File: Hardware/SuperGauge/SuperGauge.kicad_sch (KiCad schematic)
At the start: 1 part

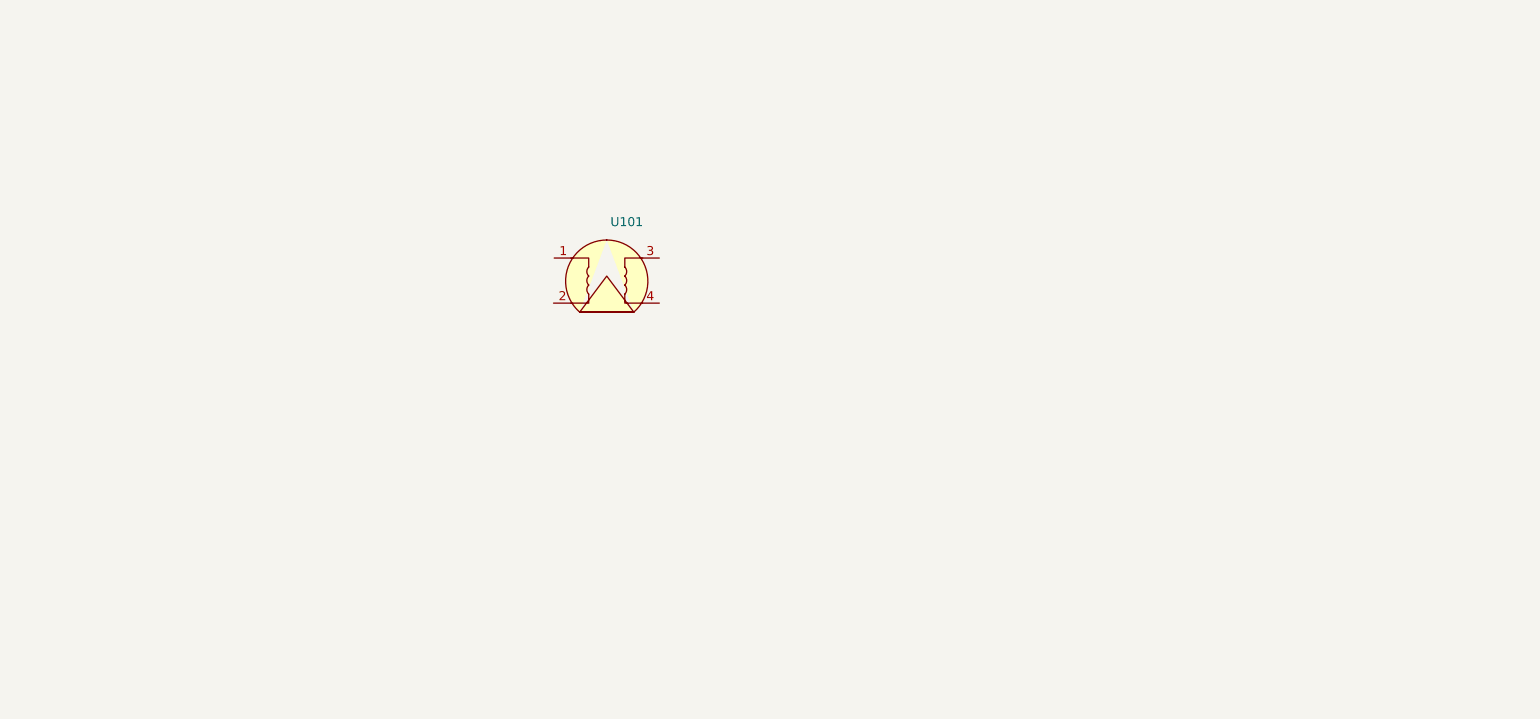
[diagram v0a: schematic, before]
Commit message: Added in MCU
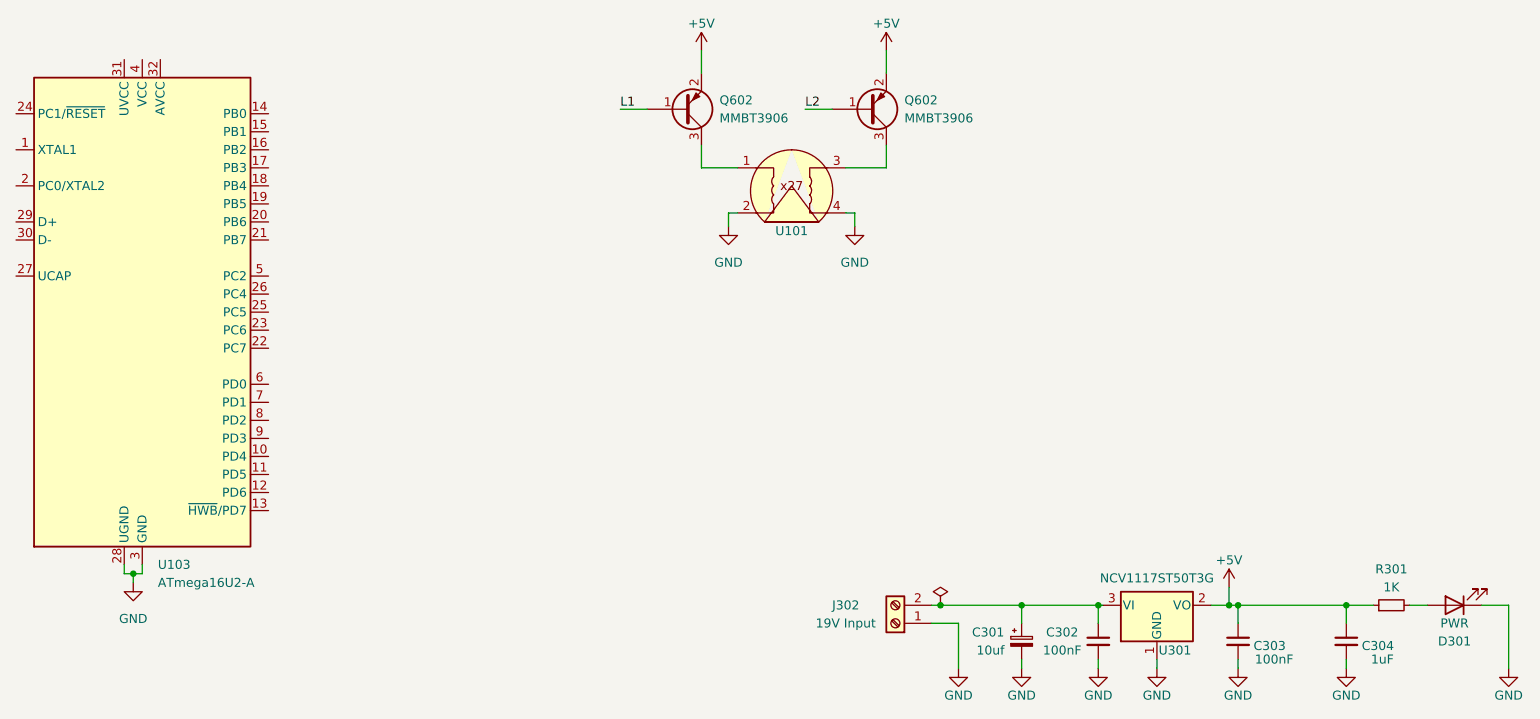
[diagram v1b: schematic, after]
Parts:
- added C301: 10uf, Capacitor_SMD:CP_Elec_4x3, symbol Device:C_Polarized_Small
- added C302, C303: 100nF, Capacitor_SMD:C_0805_2012Metric, symbol Device:C_Small
- added C304: 1uF, Capacitor_SMD:C_0805_2012Metric, symbol Device:C_Small
- added D301: PWR, LED_SMD:LED_0805_2012Metric, symbol Device:LED
- added J302: 19V Input, TerminalBlock_Phoenix:TerminalBlock_Phoenix_MKDS-3-2-5.08_1x02_P5.08mm_Horizontal, symbol Connector:Screw_Terminal_01x02
- added Q602 (x2): MMBT3906, Package_TO_SOT_SMD:SOT-23, symbol Transistor_BJT:MMBT3906
- added R301: 1K, Resistor_SMD:R_0805_2012Metric, symbol Device:R_Small
- added U103: ATmega16U2-A, Package_QFP:TQFP-32_7x7mm_P0.8mm, symbol MCU_Microchip_ATmega:ATmega16U2-A
- added U301: NCV1117ST50T3G, Package_TO_SOT_SMD:SOT-223, symbol Regulator_Linear:LM1117-5.0
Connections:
- net at U101.1: now also Q602.3 (C)
- net GND: now reaches U101.2
- net GND: now also U101.4, C301.2, C302.2, C303.2, C304.2, D301.1 (K), J302.1 (Pin_1), U103.28 (UGND), U103.3 (GND), U301.1 (GND)
- net at U101.3: now also Q602.3 (C)
- new net: C301.1, C302.1, J302.2 (Pin_2), U301.3 (VI)
- new net: D301.2 (A), R301.2
- new net +5V: C303.1, C304.1, Q602.2 (E), Q602.2 (E), R301.1, U301.2 (VO)
- new net L1: Q602.1 (B)
- new net L2: Q602.1 (B)

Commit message: More stuff
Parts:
- removed J302: 19V Input, TerminalBlock_Phoenix:TerminalBlock_Phoenix_MKDS-3-2-5.08_1x02_P5.08mm_Horizontal, symbol Connector:Screw_Terminal_01x02
- added D102, D103: BACKLIGHTING, LED_THT:LED_D5.0mm_Clear, symbol Device:LED
- added D301: STAT, LED_SMD:LED_0805_2012Metric, symbol Device:LED
- added H101, H102: MountingHole, MountingHole:MountingHole_2.5mm, symbol Mechanical:MountingHole
- added J102: MainConn, Connector_JST:JST_EH_B5B-EH-A_1x05_P2.50mm_Vertical, symbol Connector:Conn_01x05_Pin
- added R301 (x3): 1K, Resistor_SMD:R_0805_2012Metric, symbol Device:R_Small
- U103: value ATmega16U2-A -> ATmega16U2
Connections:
- net +5V: now also U103.4 (VCC), J102.4 (Pin_4), R301.1, R301.1
- net GND: now also D102.1 (K), D103.1 (K), D301.1 (K), J102.1 (Pin_1)
- net +12V: now reaches C301.1, C302.1, U301.3 (VI)
- net +12V: now also J102.5 (Pin_5)
- net at U103.6 (PD0): now also R301.1
- new net: D301.2 (A), R301.2
- new net: D102.2 (A), R301.2
- new net: D103.2 (A), R301.2
- new net SCL: J102.2 (Pin_2)
- new net SDA: J102.3 (Pin_3)
- no-connect marks 0 -> 2
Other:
- moved on the sheet: C304, D301, R301

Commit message: More PCB stuff
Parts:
- added C203, C204: 22pf, Capacitor_SMD:C_0603_1608Metric, symbol Device:C_Small
- added C303: 1u, Capacitor_SMD:C_0805_2012Metric, symbol Device:C_Small
- added J101: USBC, Connector_USB:USB_C_Receptacle_XKB_U262-16XN-4BVC11, symbol Connector:USB_C_Receptacle_USB2.0
- added R106, R107: 5K1, Resistor_SMD:R_0805_2012Metric, symbol Device:R_Small
- added Y101: Crystal_GND24, Crystal:Crystal_SMD_3225-4Pin_3.2x2.5mm, symbol Device:Crystal_GND24
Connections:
- net +5V: now also U103.32 (AVCC), J101.A4 (VBUS), J101.A9 (VBUS), J101.B4 (VBUS), J101.B9 (VBUS)
- net GND: now also C203.2, C204.2, C303.2, J101.A1 (GND), J101.A12 (GND), J101.B1 (GND), J101.B12 (GND), J101.S1 (SHIELD), R106.1, R107.1, Y101.2, Y101.4
- net XTAL1: now reaches U103.1 (XTAL1)
- net XTAL1: now also C204.1, Y101.3
- net XTAL2: now reaches U103.2 (PC0/XTAL2)
- net XTAL2: now also C203.1, Y101.1
- net at U103.27 (UCAP): now also C303.1
- net USB+: now reaches U103.29 (D+)
- net USB+: now also J101.A6 (D+), J101.B6 (D+)
- net USB-: now reaches U103.30 (D-)
- net USB-: now also J101.A7 (D-), J101.B7 (D-)
- new net: J101.A5 (CC1), R107.2
- new net: J101.B5 (CC2), R106.2
- no-connect marks 2 -> 4
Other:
- note added: "16pf = (22pf)/2+5pf"
- note added: "Consider not lol"
- note added: "USB"
- moved on the sheet: C303, D301, R301, U103

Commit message: Stuff
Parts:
- removed H101, H102: MountingHole, MountingHole:MountingHole_2.5mm, symbol Mechanical:MountingHole
- added J201: Tag Connect, Connector:Tag-Connect_TC2050-IDC-FP_2x05_P1.27mm_Vertical, symbol Connector_Generic:Conn_02x05_Odd_Even
- added R301 (x2): 22R, Resistor_SMD:R_0805_2012Metric, symbol Device:R_Small
- added R301: 10k, Resistor_SMD:R_0805_2012Metric, symbol Device:R_Small
- U103: LCSC# (none) -> C59019
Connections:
- net +5V: now also U103.31 (UVCC), J201.2 (Pin_2), R301.2
- net GND: now also J201.10 (Pin_10)
- net L1: now also U103.7 (PD1)
- net L2: now also U103.8 (PD2)
- net USB+: now also R301.1; no longer U103.29 (D+)
- net USB-: now also R301.1; no longer U103.30 (D-)
- net ICSP_SCK: now reaches U103.15 (PB1)
- net ICSP_SCK: now also J201.7 (Pin_7)
- net ICSP_MOSI: now reaches U103.16 (PB2)
- net ICSP_MOSI: now also J201.1 (Pin_1)
- net ICSP_MISO: now reaches U103.17 (PB3)
- net ICSP_MISO: now also J201.9 (Pin_9)
- net ICSP_RST: now reaches U103.24 (PC1/~{RESET})
- net ICSP_RST: now also J201.5 (Pin_5), R301.1
- new net: R301.2, U103.30 (D-)
- new net: R301.2, U103.29 (D+)
- no-connect marks 4 -> 7
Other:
- note removed: "Consider not lol"
- moved on the sheet: C203, C204, C301, C302, C303, C304, D301, J102, Q602, R301, U101, U103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

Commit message: Bump design slightly
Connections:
- net GND: now also U101.3; no longer U101.4
- net at Q602.3 (C): now also U101.4; no longer U101.3
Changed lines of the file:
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@@
   )
   (symbol (lib_id "power:GND") (at 156.21 53.34 0) (unit 1)
-    (in_bom yes) (on_board yes) (dnp no) (fields_autoplaced)
+    (in_bom yes) (on_board yes) (dnp no)
     (property "Reference" "#PWR0112" (at 156.21 59.69 0)
       (effects (font (size 1.27 1.27)) hide)
     )
-    (property "Value" "GND" (at 156.21 58.42 0)
+    (property "Value" "GND" (at 156.21 57.15 0)
       (effects (font (size 1.27 1.27)))
     )
@@
       (effects (font (size 1.27 1.27)) hide)
     )
-    (property "Datasheet" "https://4tronix.co.uk/zeropoint/x27_spec.pdf" (at 147.32 47.625 0)
+    (property "Datasheet" "http://agr.ucoz.lv/files/SP_X27_e_C.pdf" (at 147.32 47.625 0)
       (effects (font (size 1.27 1.27)) hide)
     )
@@
   )
   (symbol (lib_id "power:GND") (at 138.43 53.34 0) (unit 1)
-    (in_bom yes) (on_board yes) (dnp no) (fields_autoplaced)
+    (in_bom yes) (on_board yes) (dnp no)
     (property "Reference" "#PWR0111" (at 138.43 59.69 0)
       (effects (font (size 1.27 1.27)) hide)
     )
-    (property "Value" "GND" (at 138.43 58.42 0)
-      (effects (font (size 1.27 1.27)))
-    )
+    (property "Value" "GND" (at 138.43 57.15 0)
+      (effects (font (size 1.27 1.27)))
+    )

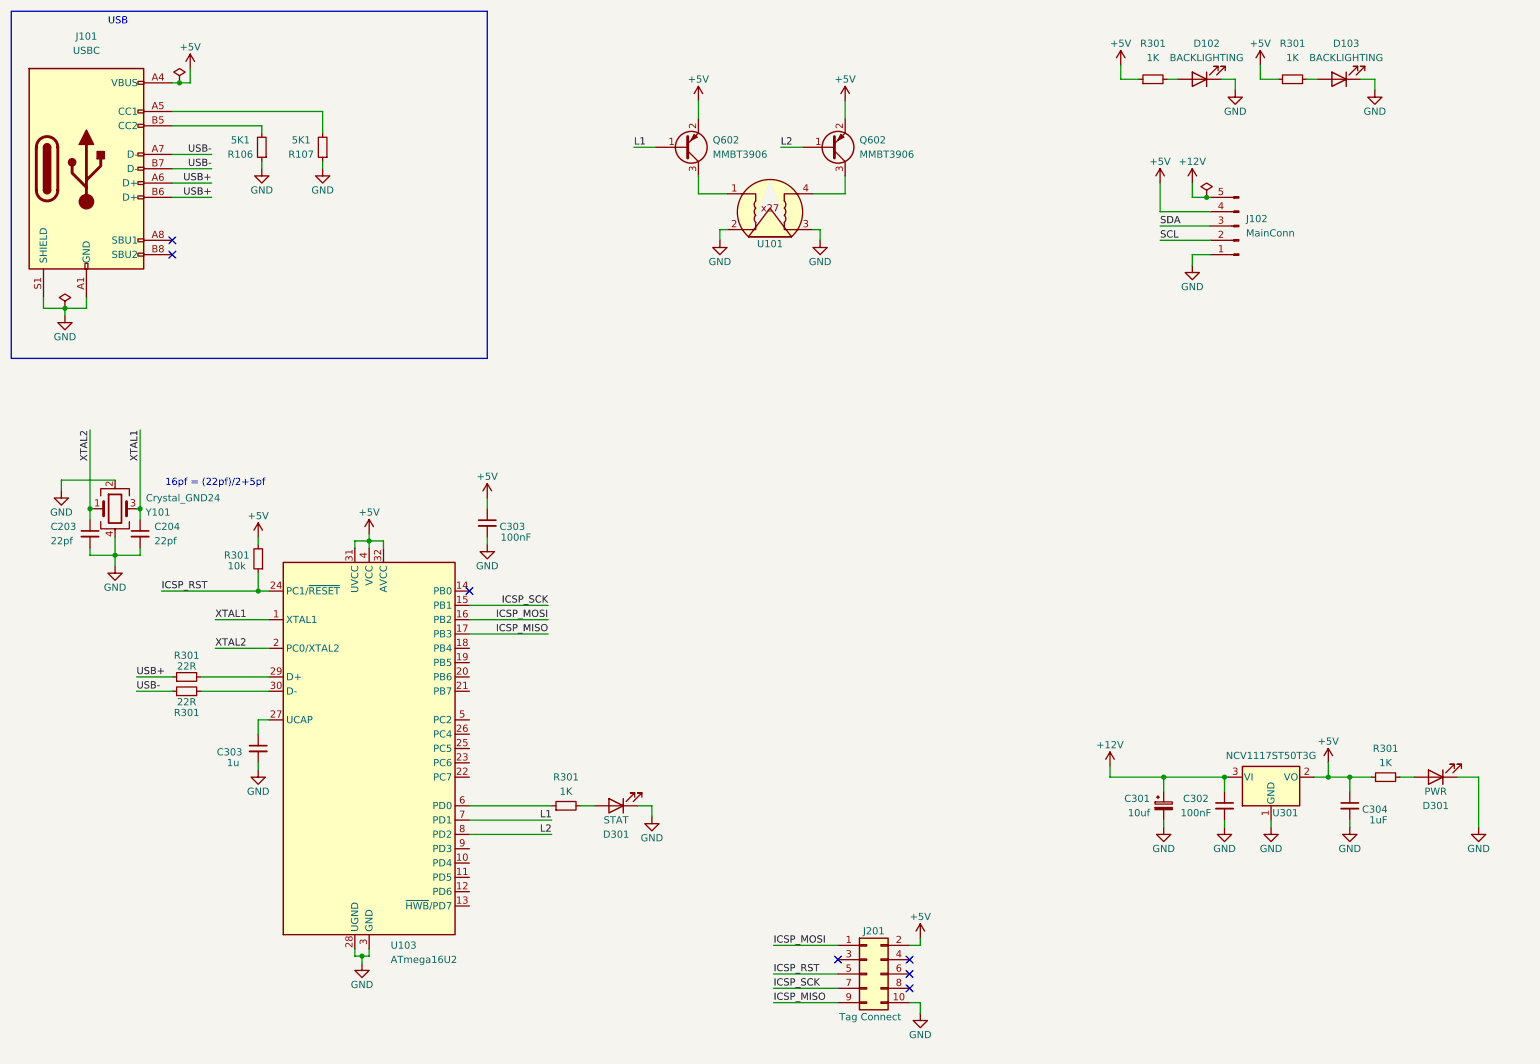
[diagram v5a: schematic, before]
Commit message: Add motor driver
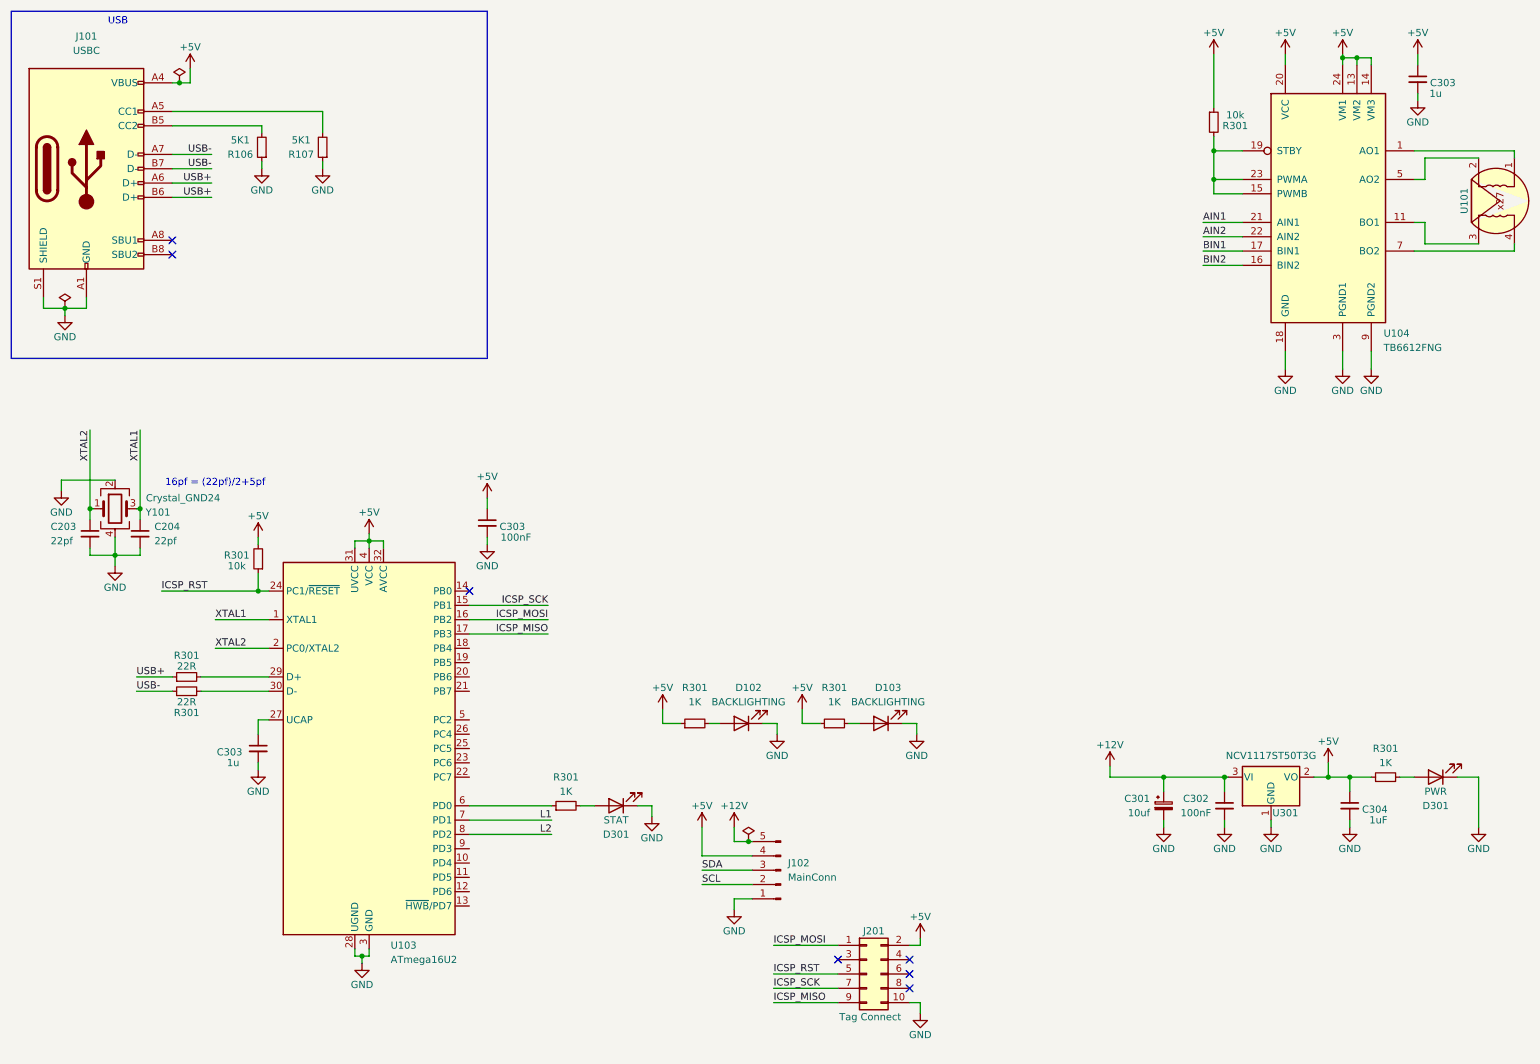
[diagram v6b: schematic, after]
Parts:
- removed Q602 (x2): MMBT3906, Package_TO_SOT_SMD:SOT-23, symbol Transistor_BJT:MMBT3906
- added C303: 1u, Capacitor_SMD:C_0805_2012Metric, symbol Device:C_Small
- added R301: 10k, Resistor_SMD:R_0805_2012Metric, symbol Device:R_Small
- added U104: TB6612FNG, Package_SO:SSOP-24_5.3x8.2mm_P0.65mm, symbol Driver_Motor:TB6612FNG
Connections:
- net +5V: now also C303.1, R301.1, U104.13 (VM2), U104.14 (VM3), U104.20 (VCC), U104.24 (VM1)
- net GND: now also C303.2, U104.10 (PGND2), U104.18 (GND), U104.3 (PGND1), U104.4 (PGND1), U104.9 (PGND2); no longer U101.2, U101.3
- net at U101.1: now also U104.1 (AO1), U104.2 (AO1)
- net at U101.4: now also U104.7 (BO2), U104.8 (BO2)
- new net: U101.2, U104.5 (AO2), U104.6 (AO2)
- new net: U101.3, U104.11 (BO1), U104.12 (BO1)
- new net: R301.2, U104.15 (PWMB), U104.19 (STBY), U104.23 (PWMA)
- new net AIN1: U104.21 (AIN1)
- new net AIN2: U104.22 (AIN2)
- new net BIN1: U104.17 (BIN1)
- new net BIN2: U104.16 (BIN2)
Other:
- moved on the sheet: D102, D103, J102, R301

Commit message: Connect all
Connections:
- net AIN1: now also U103.5 (PC2)
- net AIN2: now also U103.26 (PC4)
- net BIN1: now also U103.25 (PC5)
- net BIN2: now also U103.23 (PC6)
- net SCL: now also U103.18 (PB4)
- net SDA: now also U103.19 (PB5)
- no-connect marks 7 -> 15
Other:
- note added: "Tie PWM LOW (always enable max speed)"
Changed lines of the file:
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@@
   (junction (at 246.38 148.59) (diameter 0) (color 0 0 0 0)
   )
+  (no_connect (at 93.98 130.81))
   (no_connect (at 93.98 115.57))
+  (no_connect (at 93.98 168.91))
   (no_connect (at 159.385 180.975))
   (no_connect (at 172.085 183.515))
+  (no_connect (at 93.98 171.45))
+  (no_connect (at 93.98 133.35))
+  (no_connect (at 93.98 166.37))
   (no_connect (at 41.275 55.88))
   (no_connect (at 41.275 53.34))
   (no_connect (at 172.085 186.055))
+  (no_connect (at 93.98 163.83))
   (no_connect (at 172.085 180.975))
+  (no_connect (at 93.98 161.29))
+  (no_connect (at 93.98 148.59))
   (wire (pts (xy 251.46 20.955) (xy 254 20.955))
     (stroke (width 0) (type default))
@@
     (stroke (width 0) (type default))
   )
+  (wire (pts (xy 93.98 128.27) (xy 107.95 128.27))
+    (stroke (width 0) (type default))
+  )
   (wire (pts (xy 67.945 40.64) (xy 67.945 39.37))
     (stroke (width 0) (type default))
@@
     (stroke (width 0) (type default))
   )
+  (wire (pts (xy 93.98 143.51) (xy 107.95 143.51))
+    (stroke (width 0) (type default))
+  )
   (wire (pts (xy 126.365 153.67) (xy 126.365 155.575))
     (stroke (width 0) (type default))
@@
     (stroke (width 0) (type default))
   )
+  (wire (pts (xy 93.98 140.97) (xy 107.95 140.97))
+    (stroke (width 0) (type default))
+  )
   (wire (pts (xy 217.17 157.48) (xy 217.17 156.21))
     (stroke (width 0) (type default))
@@
     (stroke (width 0) (type default))
   )
+  (wire (pts (xy 93.98 125.73) (xy 107.95 125.73))
+    (stroke (width 0) (type default))
+  )
+  (wire (pts (xy 93.98 138.43) (xy 107.95 138.43))
+    (stroke (width 0) (type default))
+  )
   (wire (pts (xy 42.545 25.4) (xy 44.45 25.4))
     (stroke (width 0) (type default))
@@
     (stroke (width 0) (type default))
   )
+  (wire (pts (xy 93.98 146.05) (xy 107.95 146.05))
+    (stroke (width 0) (type default))
+  )
   (wire (pts (xy 56.515 138.43) (xy 56.515 140.97))
     (stroke (width 0) (type default))
@@
     (stroke (width 0) (type default))
   )
+  (text "Tie PWM LOW\n(always enable max speed)" (at 198.755 45.085 0)
+    (effects (font (size 1.27 1.27)) (justify left bottom))
+  )
   (text "USB" (at 29.845 15.24 0)
     (effects (font (size 1.27 1.27)) (justify left bottom))
@@
     (effects (font (size 1.27 1.27)) (justify right bottom))
   )
+  (label "AIN1" (at 107.95 138.43 180) (fields_autoplaced)
+    (effects (font (size 1.27 1.27)) (justify right bottom))
+  )
   (label "ICSP_MOSI" (at 147.955 178.435 0) (fields_autoplaced)
     (effects (font (size 1.27 1.27)) (justify left bottom))
@@
     (effects (font (size 1.27 1.27)) (justify left bottom))
   )
+  (label "SCL" (at 107.95 125.73 180) (fields_autoplaced)
+    (effects (font (size 1.27 1.27)) (justify right bottom))
+  )
   (label "SCL" (at 135.255 167.64 0) (fields_autoplaced)
     (effects (font (size 1.27 1.27)) (justify left bottom))
@@
     (effects (font (size 1.27 1.27)) (justify left bottom))
   )
+  (label "BIN2" (at 107.95 146.05 180) (fields_autoplaced)
+    (effects (font (size 1.27 1.27)) (justify right bottom))
+  )
   (label "USB-" (at 48.26 38.1 180) (fields_autoplaced)
     (effects (font (size 1.27 1.27)) (justify right bottom))
@@
     (effects (font (size 1.27 1.27)) (justify right bottom))
   )
+  (label "AIN2" (at 107.95 140.97 180) (fields_autoplaced)
+    (effects (font (size 1.27 1.27)) (justify right bottom))
+  )
+  (label "SDA" (at 107.95 128.27 180) (fields_autoplaced)
+    (effects (font (size 1.27 1.27)) (justify right bottom))
+  )
   (label "ICSP_MOSI" (at 107.95 120.65 180) (fields_autoplaced)
     (effects (font (size 1.27 1.27)) (justify right bottom))
@@
     (effects (font (size 1.27 1.27)) (justify left bottom))
   )
+  (label "BIN1" (at 107.95 143.51 180) (fields_autoplaced)
+    (effects (font (size 1.27 1.27)) (justify right bottom))
+  )
   (label "USB+" (at 34.925 130.81 0) (fields_autoplaced)
